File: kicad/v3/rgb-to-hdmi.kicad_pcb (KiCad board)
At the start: 2 copper layers, 65 x 30 mm, 31 parts, among them P1 CONN_02X20, P2 CONN_01X03, P3 CONN_01X06, P4 CONN_01X02, P5 CONN_01X06, P6 CONN_01X02, P7 Conn_01x01, SW1 SW_PUSH, SW2 SW_PUSH, SW3 SW_PUSH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

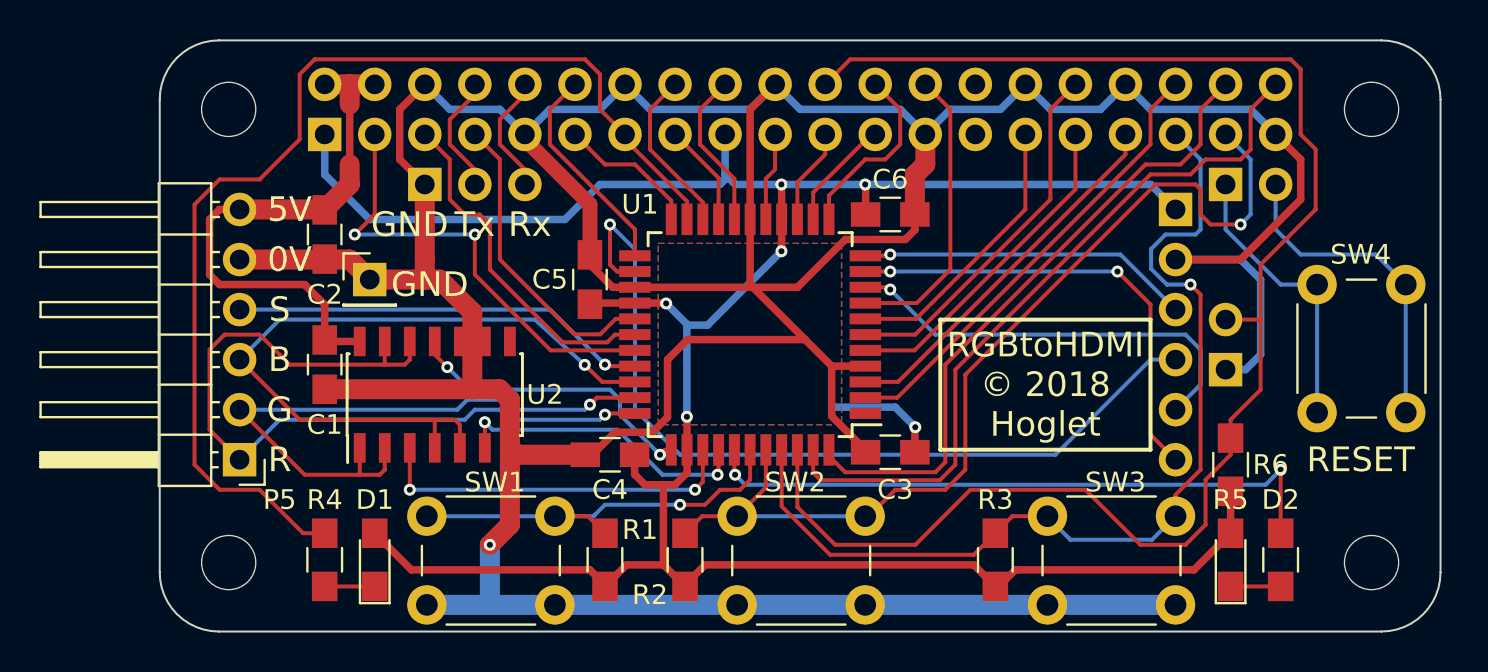
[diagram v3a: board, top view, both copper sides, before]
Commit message: KiCad: Removed SW1Out passthrough to save a produce term
Change-Id: I7cc547a21f411a16182b2e27dbd37bbfed956f1c
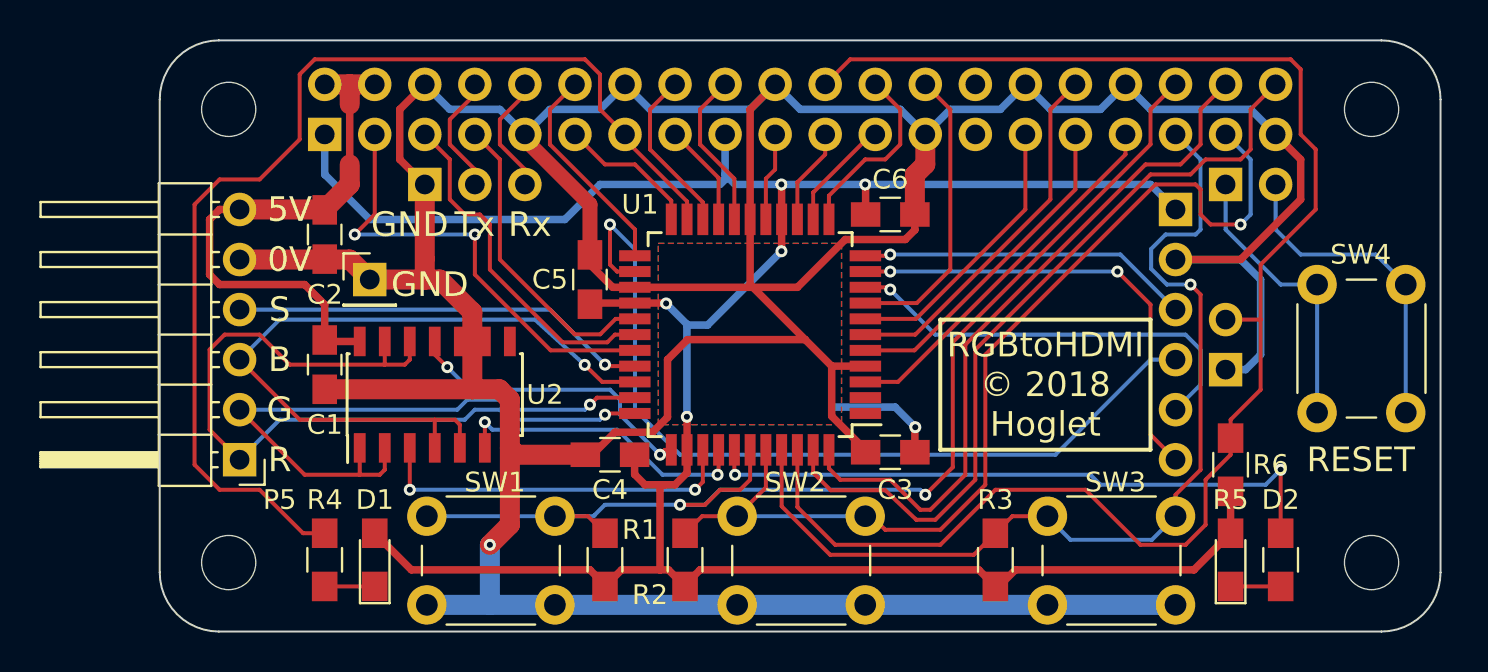
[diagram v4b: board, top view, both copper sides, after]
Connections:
- R1 pad 2: /SW1 -> /GPIO16
- SW1 pad 2: /SW1 -> /GPIO16
- U1 pad 2: /GPIO16 -> (no net)
- U1 pad 39: /SW1 -> /GPIO16
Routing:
- net /GPIO16: track 23.4 -> 61.3 mm, vias 0 -> 2
- net /SW1: track 22.4 -> 0.00 mm, vias 1 -> 0
- net /GPIO20: track 32.9 -> 36.1 mm
- net /GPIO21: track 37.1 -> 39.8 mm
- net /GPIO26: track 49.2 -> 51.0 mm

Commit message: KiCad: Brought gpio0/1 into use as extra cpld inputs
Change-Id: I84108de621164400689d12acfefccd9b05fdbe75
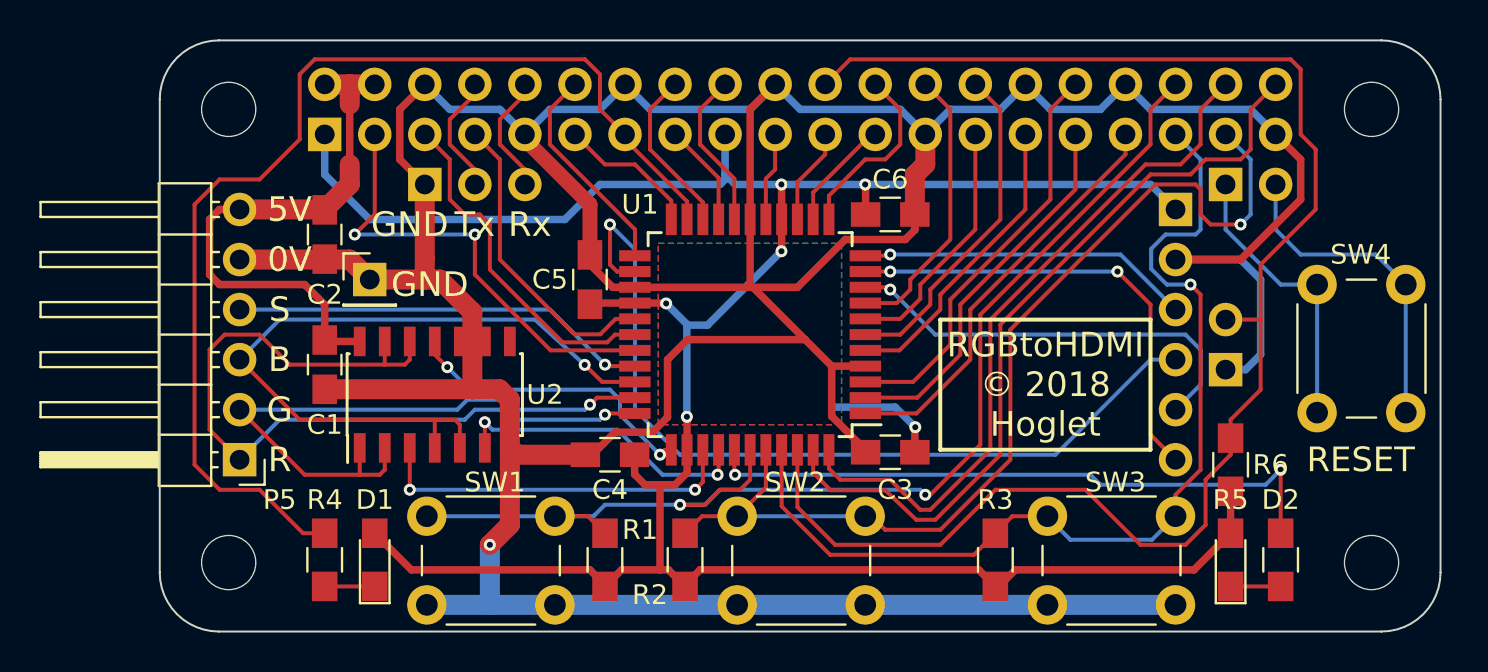
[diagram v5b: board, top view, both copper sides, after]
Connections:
- P1 pad 27: (no net) -> /GPIO0
- P1 pad 28: (no net) -> /GPIO1
- U1 pad 1: (no net) -> /GPIO13
- U1 pad 2: (no net) -> /GPIO6
- U1 pad 3: /GPIO13 -> /GPIO12
- U1 pad 5: /GPIO6 -> /GPIO5
- U1 pad 6: /GPIO12 -> /GPIO1
- U1 pad 7: /GPIO5 -> /GPIO0
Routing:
- net /GPIO1: track 0.00 -> 17.1 mm
- net /GPIO0: track 0.00 -> 12.7 mm
- net /GPIO6: track 16.8 -> 19.3 mm
- net /GPIO12: track 18.6 -> 20.9 mm
- net /GPIO13: track 19.0 -> 21.1 mm
- net /GPIO5: track 14.2 -> 15.3 mm
- net /GPIO7: track 14.9 -> 14.3 mm

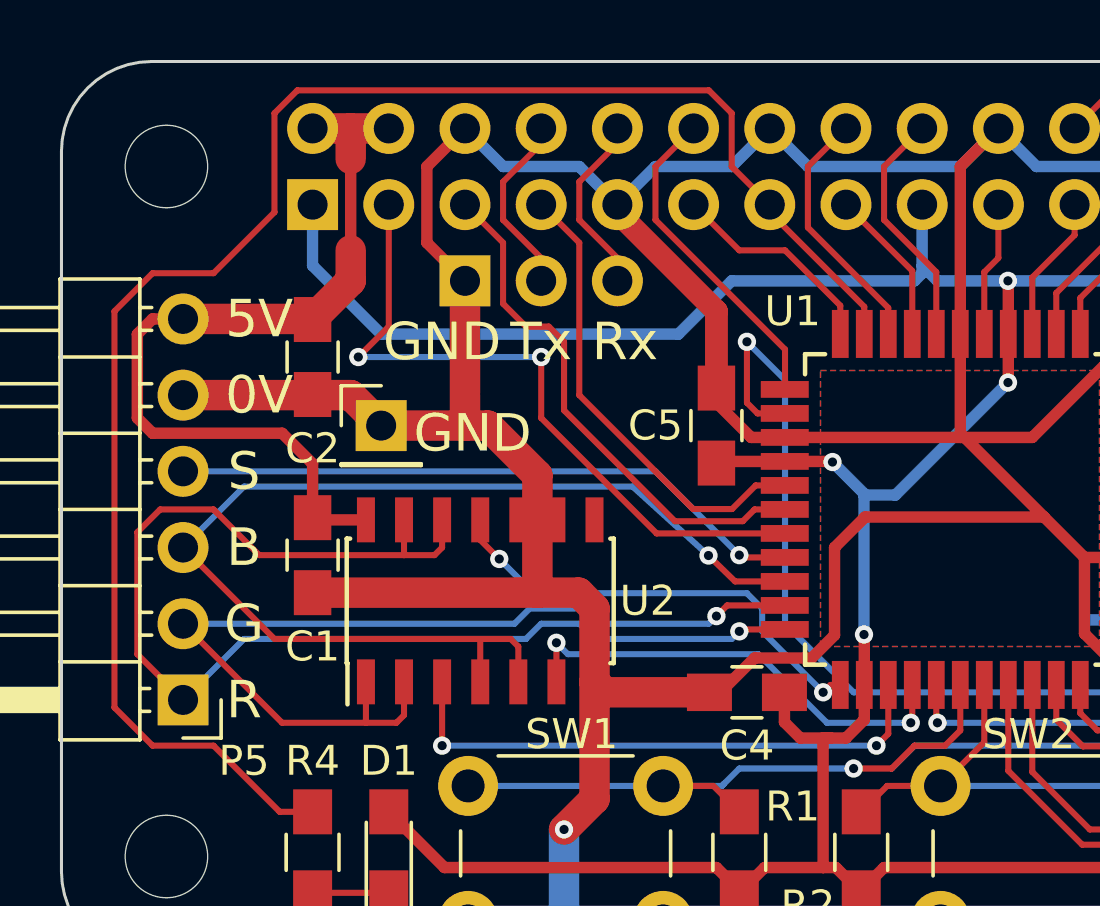
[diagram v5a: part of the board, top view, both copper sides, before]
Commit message: KiCad: Juggled R/G/B/S inputs so GSR connects to GPIO18
Change-Id: Ib20cb67e3db2335fc415cc18dea77bd197516aa8
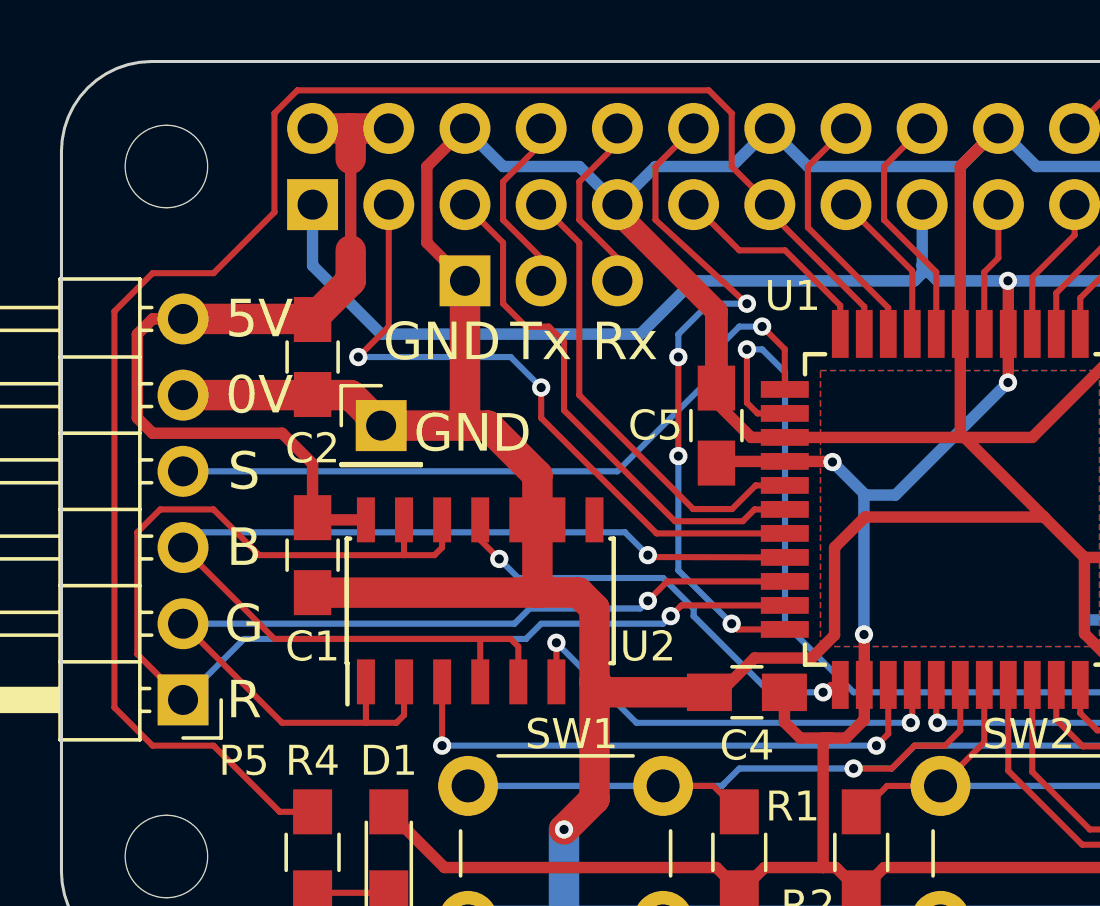
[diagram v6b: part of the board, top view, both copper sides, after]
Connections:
- U1 pad 23: /GPIO18 -> /SYNC
- U1 pad 30: /SYNC -> /BLUE
- U1 pad 31: /BLUE -> /GREEN
- U1 pad 32: /GREEN -> /RED
- U1 pad 33: /RED -> /GPIO18
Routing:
- net /GPIO18: track 11.0 -> 22.7 mm, vias 0 -> 4
- net /SYNC: track 21.2 -> 24.2 mm
- net /BLUE: track 37.3 -> 35.8 mm
- net /GPIO2: track 23.3 -> 22.7 mm

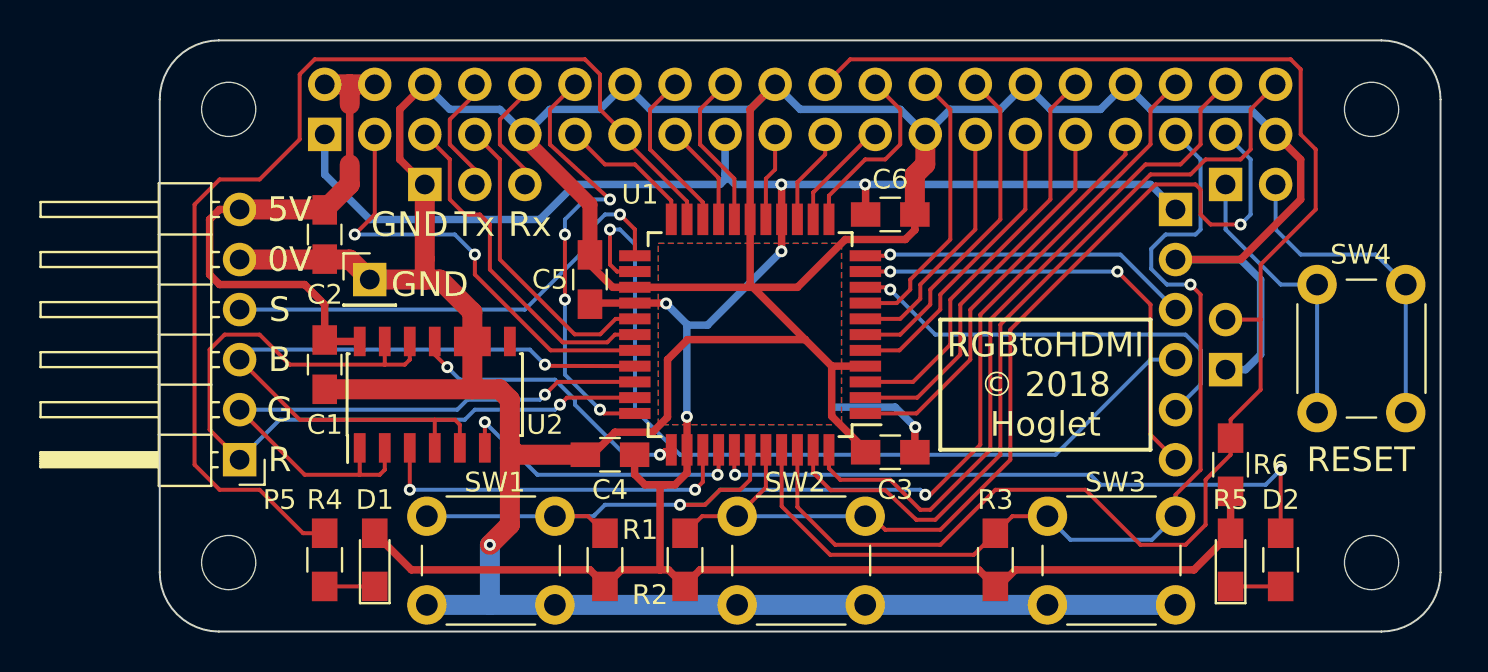
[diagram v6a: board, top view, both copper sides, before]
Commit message: KiCad: Final set of CPLD pinout changes
Change-Id: Ic3bbec75507d185d1a1419b75b4cf4d1f649dc78
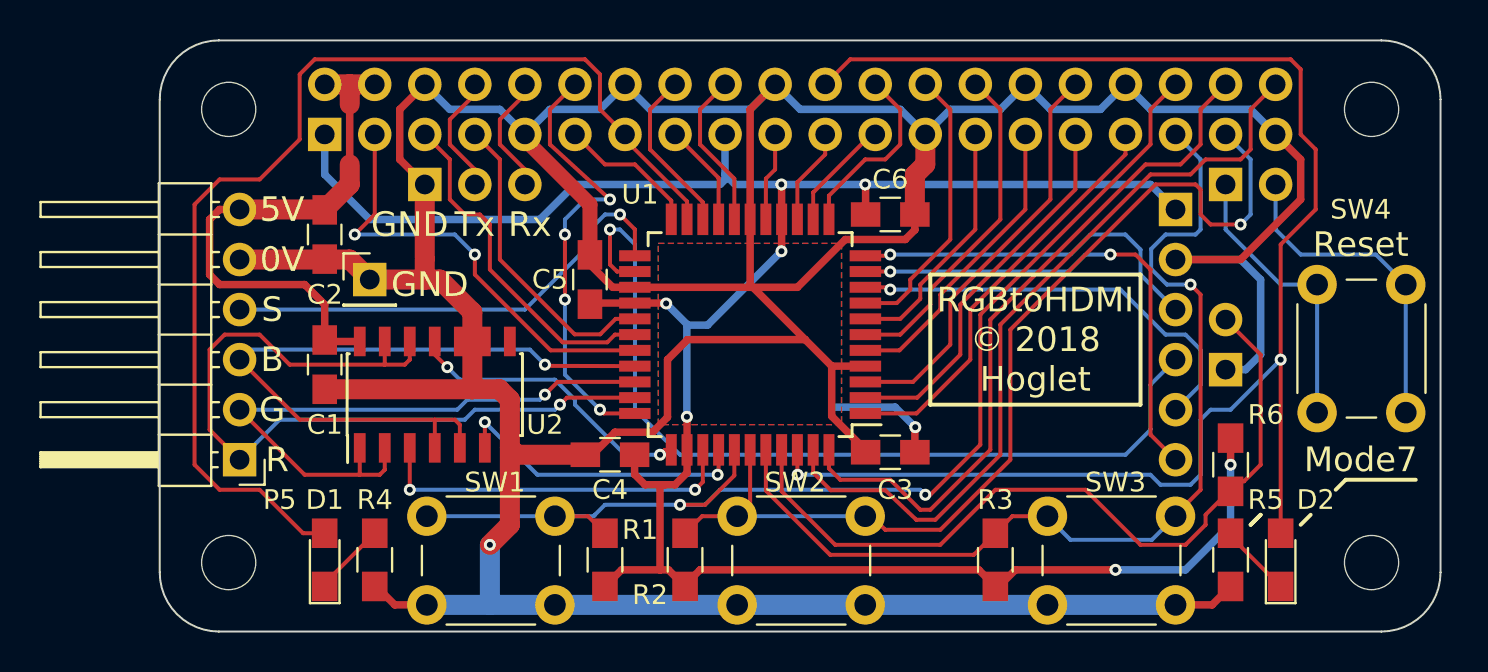
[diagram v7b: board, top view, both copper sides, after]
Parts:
- moved D1 2.54 mm to (20.9, 50.9)
- moved R4 2.54 mm to (23.4, 50.9), turned to 270 degrees
- moved D2 2.54 mm to (69.4, 50.9)
- moved R5 2.54 mm to (66.8, 50.9), turned to 270 degrees
- turned R6 to 270 degrees
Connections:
- D1 pad 2: /3V3 -> /GPIO27
- D2 pad 2: /3V3 -> /GPIO25
- P6 pad 2: /GPIO25 -> /LINK
- R4 pad 2: /GPIO27 -> GND
- R5 pad 2: /LED -> GND
- R6 pad 2: /GPIO25 -> /LINK
- U1 pad 38: /LED -> /GPIO16
- U1 pad 39: /GPIO16 -> /GPIO26
- U1 pad 40: /GPIO26 -> /GPIO19
- U1 pad 41: /GPIO19 -> /LINK
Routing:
- net /LINK: track 0.00 -> 40.2 mm
- net /LED: track 32.7 -> 0.00 mm, vias 2 -> 0
- net /3V3: track 139.8 -> 129.5 mm, vias 6 -> 8
- net GND: track 238.1 -> 244.3 mm
- net /TMS: track 24.0 -> 25.7 mm
- net /TCK: track 16.9 -> 18.5 mm
- net /TDO: track 43.5 -> 44.9 mm
- net Net-(D2-Pad1): track 2.54 -> 3.75 mm
- net Net-(D1-Pad1): track 2.54 -> 3.75 mm
- net /GPIO16: track 61.5 -> 60.6 mm
- net /GPIO25: track 79.5 -> 79.7 mm, vias 0 -> 2
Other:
- board text added: "Mode7"
- board text added: "Reset"
- board text removed: "RESET"

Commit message: KiCad: starting to prepare manufacturing files
Change-Id: Ia4f3cd37cff8fe786a41006096e8ada554b6ffb9
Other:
- rule pad_to_mask_clearance: 0 -> 0.2
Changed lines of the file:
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@@
     (links 114)
     (no_connects 0)
-    (area 12.449999 24.449999 77.550001 54.550001)
+    (area 1.450001 13.3 101.014286 60.381101)
     (thickness 1.6)
     (drawings 55)
@@
     (0 F.Cu signal)
     (31 B.Cu signal)
-    (34 B.Paste user)
-    (35 F.Paste user)
+    (34 B.Paste user hide)
+    (35 F.Paste user hide)
     (36 B.SilkS user)
     (37 F.SilkS user)
@@
     (pad_size 1.7 1.7)
     (pad_drill 1)
-    (pad_to_mask_clearance 0)
+    (pad_to_mask_clearance 0.2)
     (aux_axis_origin 0 0)
     (grid_origin 45.002 28.00096)
     (visible_elements 7FFEFFFF)
     (pcbplotparams
-      (layerselection 0x01330_80000001)
-      (usegerberextensions false)
+      (layerselection 0x010f0_80000001)
+      (usegerberextensions true)
       (excludeedgelayer true)
       (linewidth 0.100000)
@@
       (psa4output false)
       (plotreference true)
-      (plotvalue true)
+      (plotvalue false)
       (plotinvisibletext false)
       (padsonsilk false)
       (subtractmaskfromsilk false)
-      (outputformat 4)
+      (outputformat 1)
       (mirror false)
-      (drillshape 2)
+      (drillshape 0)
       (scaleselection 1)
-      (outputdirectory meta/))
+      (outputdirectory manufacturing/))
   )
   (net 0 "")
